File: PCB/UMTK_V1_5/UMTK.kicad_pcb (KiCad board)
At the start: 4 copper layers, 170 x 80 mm, 93 parts, among them J1 Motor Out, J2 ESTOP, J3 LOADCELL, J5 PJ-102BH, J8 10033526-N3212LF, Q1 Q_PNP_BEC, U1 DRV8873SPWPRQ1, U10 LM2576HVS-5, U11 SN74LVC1T45DCK, U12 SN74LVC1T45DCK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

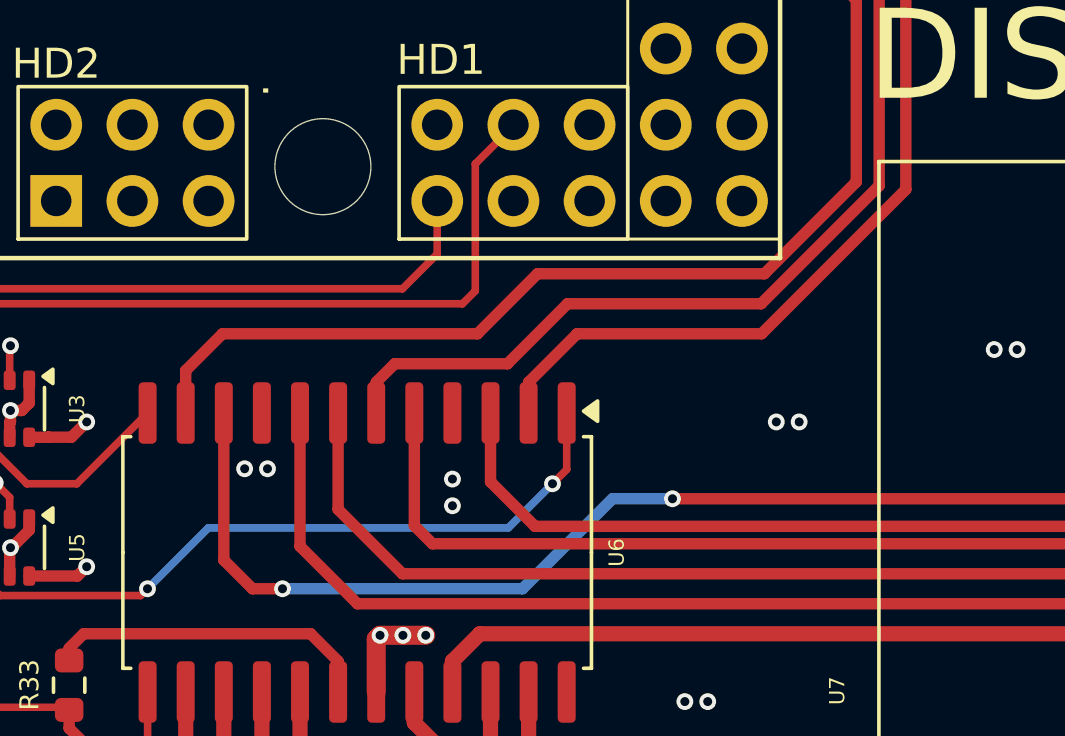
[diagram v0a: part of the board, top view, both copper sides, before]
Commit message: Debugging firmware, feature add
Added feature to disable leading zeros and turn them off.
Updating PCB, all general parts should be 0603 by default.
Add configratble decimal point location
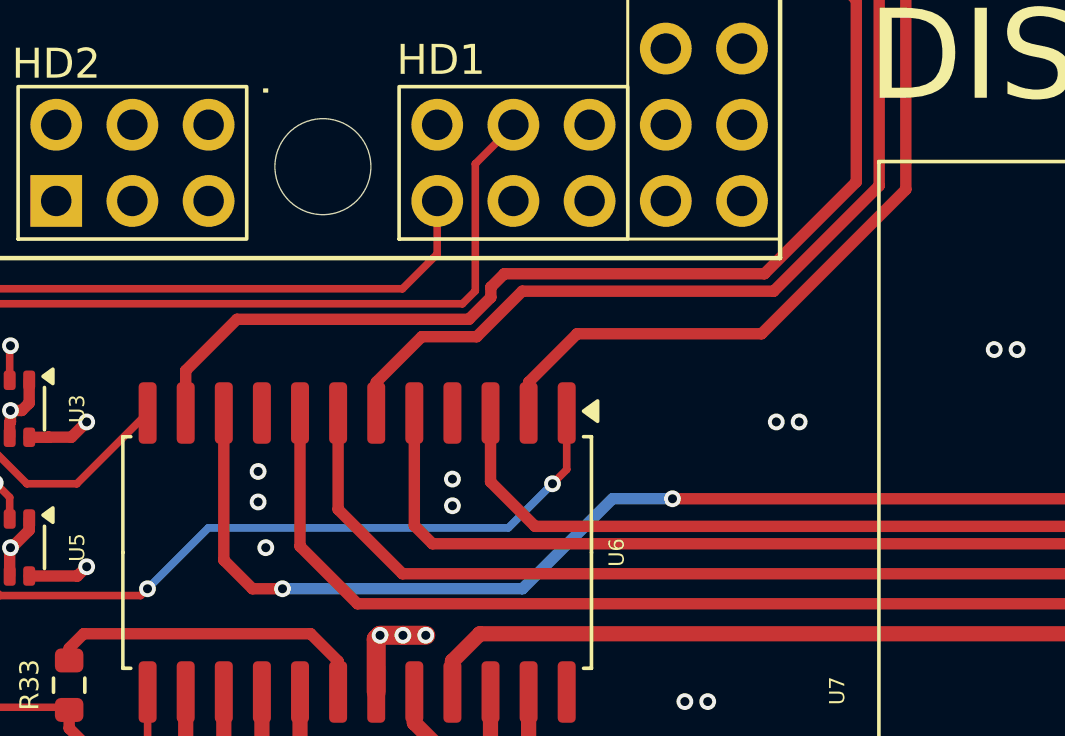
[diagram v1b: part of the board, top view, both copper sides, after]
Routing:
- net GND: vias 279 -> 280
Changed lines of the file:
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@@
 	)
 	(via
+		(at 43.942 87.63)
+		(size 0.56)
+		(drill 0.3)
+		(layers "F.Cu" "B.Cu")
+		(net 4)
+	)
+	(via
 		(at 109.347 51.562)
 		(size 0.56)
@@
 	)
 	(via
-		(at 43.238 85)
+		(at 43.688 86.106)
 		(size 0.56)
 		(drill 0.3)
@@
 	)
 	(via
-		(at 44 85)
+		(at 43.688 85.09)
 		(size 0.56)
 		(drill 0.3)
@@
 	)
 	(segment
-		(start 64.389 75.565)
-		(end 60.454 79.5)
+		(start 47.624 82.116001)
+		(end 47.624 83.141)
 		(width 0.381)
 		(layer "F.Cu")
@@
 	)
 	(segment
-		(start 52 81.5)
-		(end 48.240001 81.5)
+		(start 89 44)
+		(end 68.776 44)
 		(width 0.381)
 		(layer "F.Cu")
@@
 	)
 	(segment
-		(start 64.389 48.387)
-		(end 64.389 75.565)
+		(start 90.297 46.99)
+		(end 89.662 46.355)
 		(width 0.381)
 		(layer "F.Cu")
@@
 	)
 	(segment
-		(start 89 44)
-		(end 68.776 44)
+		(start 92.115 46.99)
+		(end 90.297 46.99)
 		(width 0.381)
 		(layer "F.Cu")
@@
 	)
 	(segment
-		(start 93.46 45.645)
-		(end 92.115 46.99)
+		(start 68.776 44)
+		(end 64.389 48.387)
 		(width 0.381)
 		(layer "F.Cu")
@@
 	)
 	(segment
-		(start 92.115 46.99)
-		(end 90.297 46.99)
+		(start 89.662 44.662)
+		(end 89 44)
 		(width 0.381)
 		(layer "F.Cu")
@@
 	)
 	(segment
-		(start 54 79.5)
-		(end 52 81.5)
+		(start 52.491 79.081)
+		(end 50.9735 80.5985)
 		(width 0.381)
 		(layer "F.Cu")
@@
 	)
 	(segment
-		(start 89.662 44.662)
-		(end 89 44)
+		(start 64.389 48.387)
+		(end 64.389 75.565)
 		(width 0.381)
 		(layer "F.Cu")
@@
 	)
 	(segment
-		(start 47.624 82.116001)
-		(end 47.624 83.141)
+		(start 49.141501 80.5985)
+		(end 47.624 82.116001)
 		(width 0.381)
 		(layer "F.Cu")
@@
 	)
 	(segment
-		(start 89.662 46.355)
-		(end 89.662 44.662)
+		(start 64.389 75.565)
+		(end 60.873 79.081)
 		(width 0.381)
 		(layer "F.Cu")
@@
 	)
 	(segment
-		(start 48.240001 81.5)
-		(end 47.624 82.116001)
+		(start 93.46 45.645)
+		(end 92.115 46.99)
 		(width 0.381)
 		(layer "F.Cu")
@@
 	)
 	(segment
-		(start 60.454 79.5)
-		(end 54 79.5)
+		(start 89.662 46.355)
+		(end 89.662 44.662)
 		(width 0.381)
 		(layer "F.Cu")
@@
 	)
 	(segment
-		(start 90.297 46.99)
-		(end 89.662 46.355)
+		(start 50.9735 80.5985)
+		(end 49.141501 80.5985)
 		(width 0.381)
 		(layer "F.Cu")
@@
 	)
 	(segment
-		(start 68.776 44)
-		(end 64.389 48.387)
+		(start 60.873 79.081)
+		(end 52.491 79.081)
 		(width 0.381)
 		(layer "F.Cu")
@@
 	)
 	(segment
-		(start 51 80.5)
-		(end 42.5 80.5)
+		(start 51.893 78.5)
+		(end 51.444501 78.948499)
 		(width 0.381)
 		(layer "F.Cu")
@@
 	)
 	(segment
-		(start 90.92 45.645)
-		(end 90.92 44.42)
+		(start 60.565 78.5)
+		(end 51.893 78.5)
 		(width 0.381)
 		(layer "F.Cu")
@@
 	)
 	(segment
-		(start 63.627 69.373)
-		(end 63.627 75.438)
+		(start 90.92 44.42)
+		(end 89.5 43)
 		(width 0.381)
 		(layer "F.Cu")
@@
 	)
 	(segment
-		(start 68.506 43)
-		(end 63.373 48.133)
+		(start 51.444501 78.948499)
+		(end 51.444501 79.287355)
 		(width 0.381)
 		(layer "F.Cu")
@@
 	)
 	(segment
-		(start 63.373 48.133)
-		(end 63.373 69.119)
+		(start 42.9825 80.0175)
+		(end 41.274 81.726)
 		(width 0.381)
 		(layer "F.Cu")
@@
 	)
 	(segment
-		(start 42.5 80.5)
-		(end 41.274 81.726)
+		(start 63.373 69.119)
+		(end 63.627 69.373)
 		(width 0.381)
 		(layer "F.Cu")
@@
 	)
 	(segment
-		(start 63.373 69.119)
-		(end 63.627 69.373)
+		(start 89.5 43)
+		(end 68.506 43)
+		(width 0.381)
+		(layer "F.Cu")
+		(net 82)
+	)
+	(segment
+		(start 51.444501 79.287355)
+		(end 50.714356 80.0175)
+		(width 0.381)
+		(layer "F.Cu")
+		(net 82)
+	)
+	(segment
+		(start 63.627 69.373)
+		(end 63.627 75.438)
 		(width 0.381)
 		(layer "F.Cu")
@@
 	)
 	(segment
-		(start 89.5 43)
-		(end 68.506 43)
+		(start 68.506 43)
+		(end 63.373 48.133)
 		(width 0.381)
 		(layer "F.Cu")
@@
 	)
 	(segment
-		(start 41.274 81.726)
-		(end 41.274 83.141)
+		(start 63.373 48.133)
+		(end 63.373 69.119)
 		(width 0.381)
 		(layer "F.Cu")
@@
 	)
 	(segment
-		(start 90.92 44.42)
-		(end 89.5 43)
+		(start 90.92 45.645)
+		(end 90.92 44.42)
 		(width 0.381)
 		(layer "F.Cu")
@@
 	)
 	(segment
-		(start 53 78.5)
-		(end 51 80.5)
+		(start 50.714356 80.0175)
+		(end 42.9825 80.0175)
 		(width 0.381)
 		(layer "F.Cu")
@@
 	)
 	(segment
-		(start 60.565 78.5)
-		(end 53 78.5)
+		(start 41.274 81.726)
+		(end 41.274 83.141)
 		(width 0.381)
 		(layer "F.Cu")

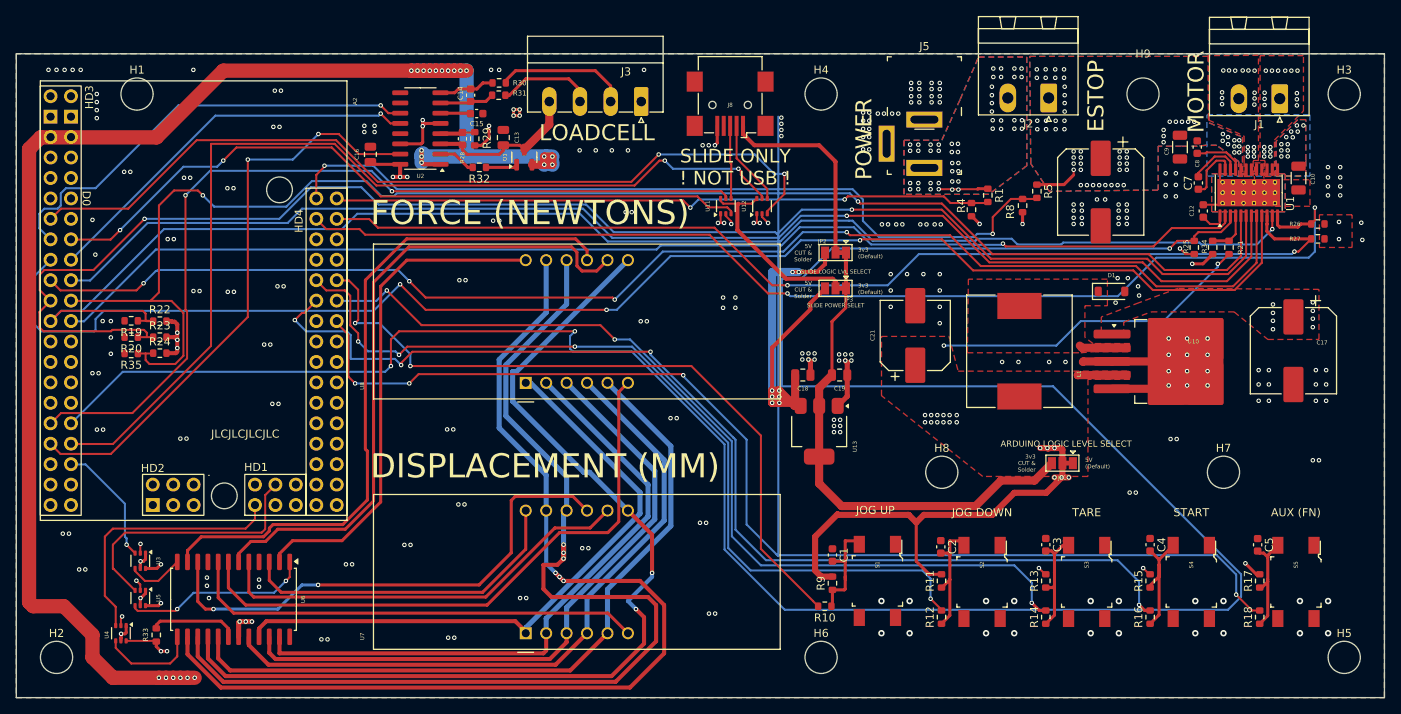
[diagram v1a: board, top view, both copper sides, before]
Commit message: Updated slide pinout, add protection, Fixed some issues
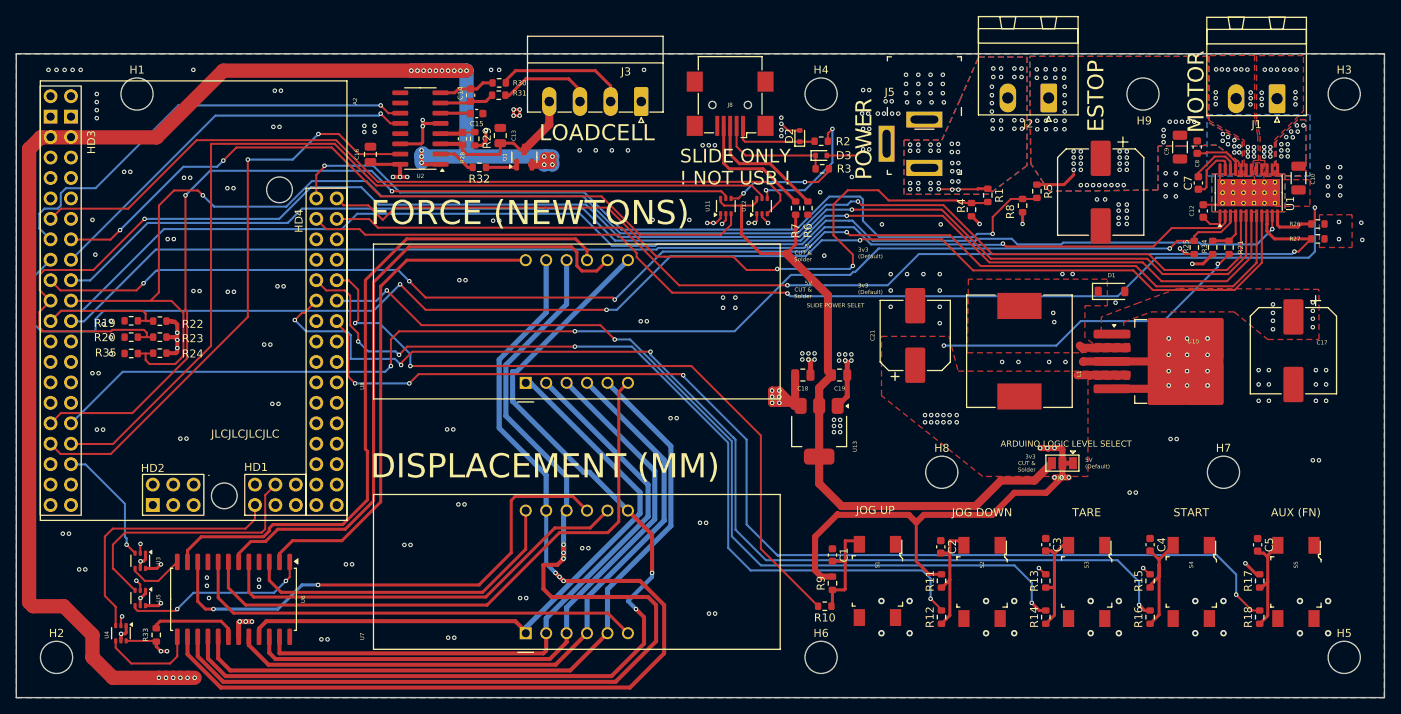
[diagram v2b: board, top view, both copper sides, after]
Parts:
- removed JP2: SlidePower, Jumper:SolderJumper-3_P1.3mm_Bridged12_Pad1.0x1.5mm
- removed JP3: Slide Logic LVL, Jumper:SolderJumper-3_P1.3mm_Bridged12_Pad1.0x1.5mm
- added D2: ZENER 5V, Diode_SMD:D_SOD-523, F.Cu at (117.3, 30.2)
- added D3: ZENER 5V, Diode_SMD:D_SOD-523, F.Cu at (120.0, 32.6)
- added R2: 1K, Resistor_SMD:R_0603_1608Metric, F.Cu at (120.0, 30.9)
- added R3: 1K, Resistor_SMD:R_0603_1608Metric, F.Cu at (120.1, 34.3)
- added R6: 0R, Resistor_SMD:R_0603_1608Metric, F.Cu at (118.4, 39.2)
- added R7: 0R, Resistor_SMD:R_0603_1608Metric, F.Cu at (116.8, 39.2)
- moved C13 0.46 mm to (80.1, 30.2)
- moved J1 0.33 mm to (176.7, 25.6)
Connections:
- J8 pad 1: /Linear Slide/SLIDE_PWR -> Net-(D2-K)
- J8 pad 2: /Linear Slide/_SLIDE_DAT_ -> Net-(D3-K)
- J8 pad 3: /Linear Slide/_SLIDE_CLK_ -> Net-(J8-D+)
- J8 pad 4: unconnected-(J8-ID-Pad4) -> Net-(J8-ID)
- J8 pad 5: GND -> unconnected-(J8-GND-Pad5)
- U11 pad 6: /Linear Slide/_SLIDE_DATA_LVL_ -> +3V3
- U12 pad 6: /Linear Slide/_SLIDE_DATA_LVL_ -> +3V3
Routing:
- net /Arduino/MOT_MODE: track 319.6 -> 157.5 mm
- net /Arduino/SW_5: track 196.2 -> 141.6 mm
- net +5V: track 302.9 -> 262.1 mm, vias 52 -> 50
- net /Linear Slide/SLIDE_PWR: track 25.2 -> 0.00 mm
- net /Linear Slide/_SLIDE_DATA_LVL_: track 24.3 -> 0.00 mm
- net +3V3: track 62.4 -> 85.0 mm
- net /Arduino/Vin_Sense: track 82.0 -> 98.5 mm
- net Net-(J8-D+): track 0.00 -> 15.6 mm
- net Net-(J8-ID): track 0.00 -> 15.6 mm
- net Net-(D3-K): track 0.00 -> 14.5 mm
- net Net-(D2-K): track 0.00 -> 10.7 mm
- net /Linear Slide/_SLIDE_DAT_: track 10.6 -> 16.7 mm, vias 0 -> 2
- net /Arduino/SLIDE_DAT: track 105.6 -> 100.6 mm, vias 2 -> 0
- net /Linear Slide/_SLIDE_CLK_: track 9.08 -> 13.9 mm, vias 0 -> 2
- net GND: track 61.2 -> 65.4 mm, vias 280 -> 269
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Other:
- board text removed: "SLIDE LOGIC LVL SELECT"
